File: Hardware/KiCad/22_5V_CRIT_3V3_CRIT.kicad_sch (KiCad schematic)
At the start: 0 parts

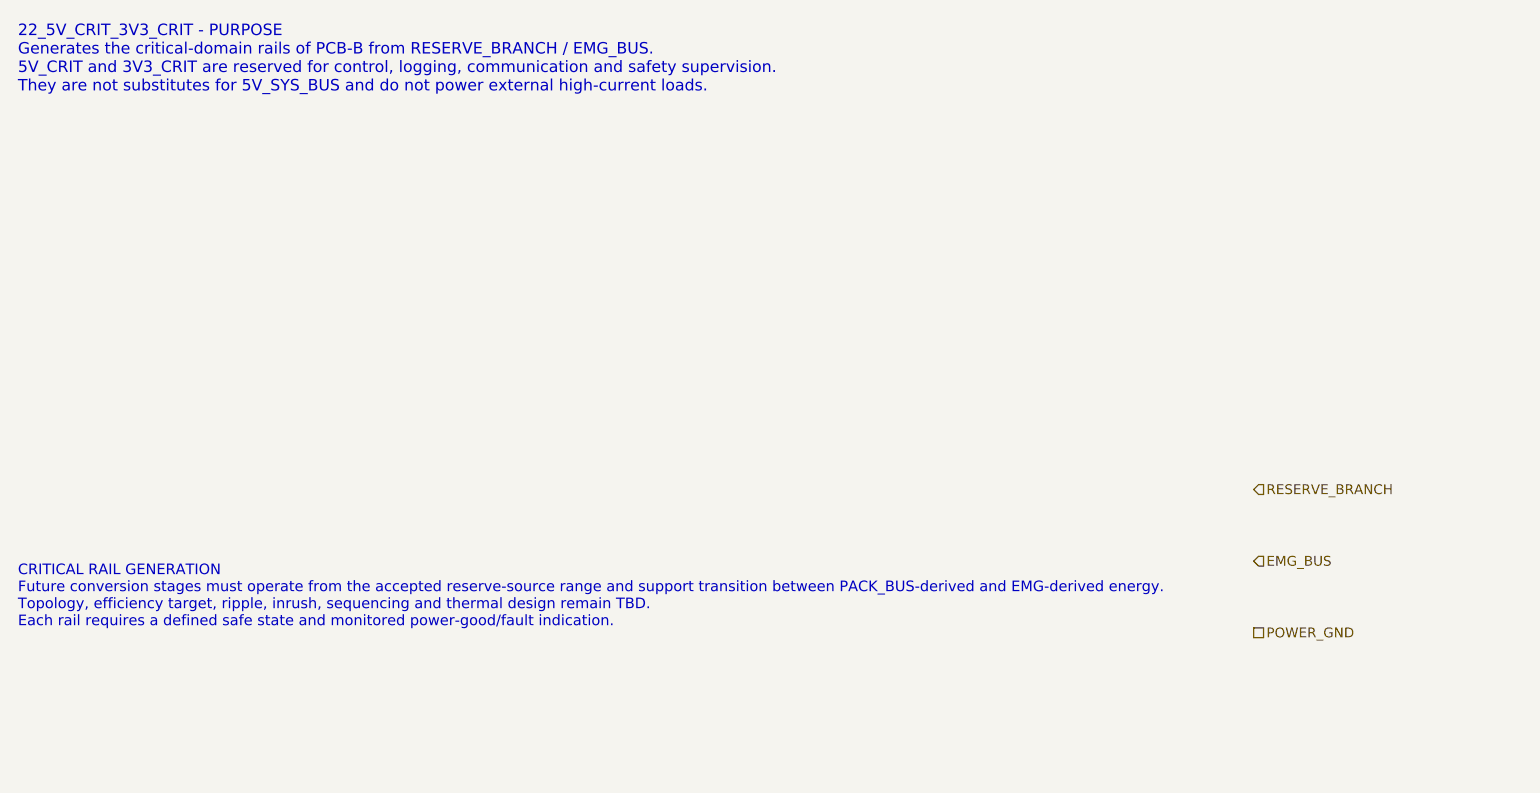
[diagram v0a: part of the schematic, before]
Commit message: hardware: align PCB-B CTRL_RESERVE interfaces
Merge PCB-B interface consistency fixes after verifying canonical names, diagnostics, and independent EXT_KILL final actions.
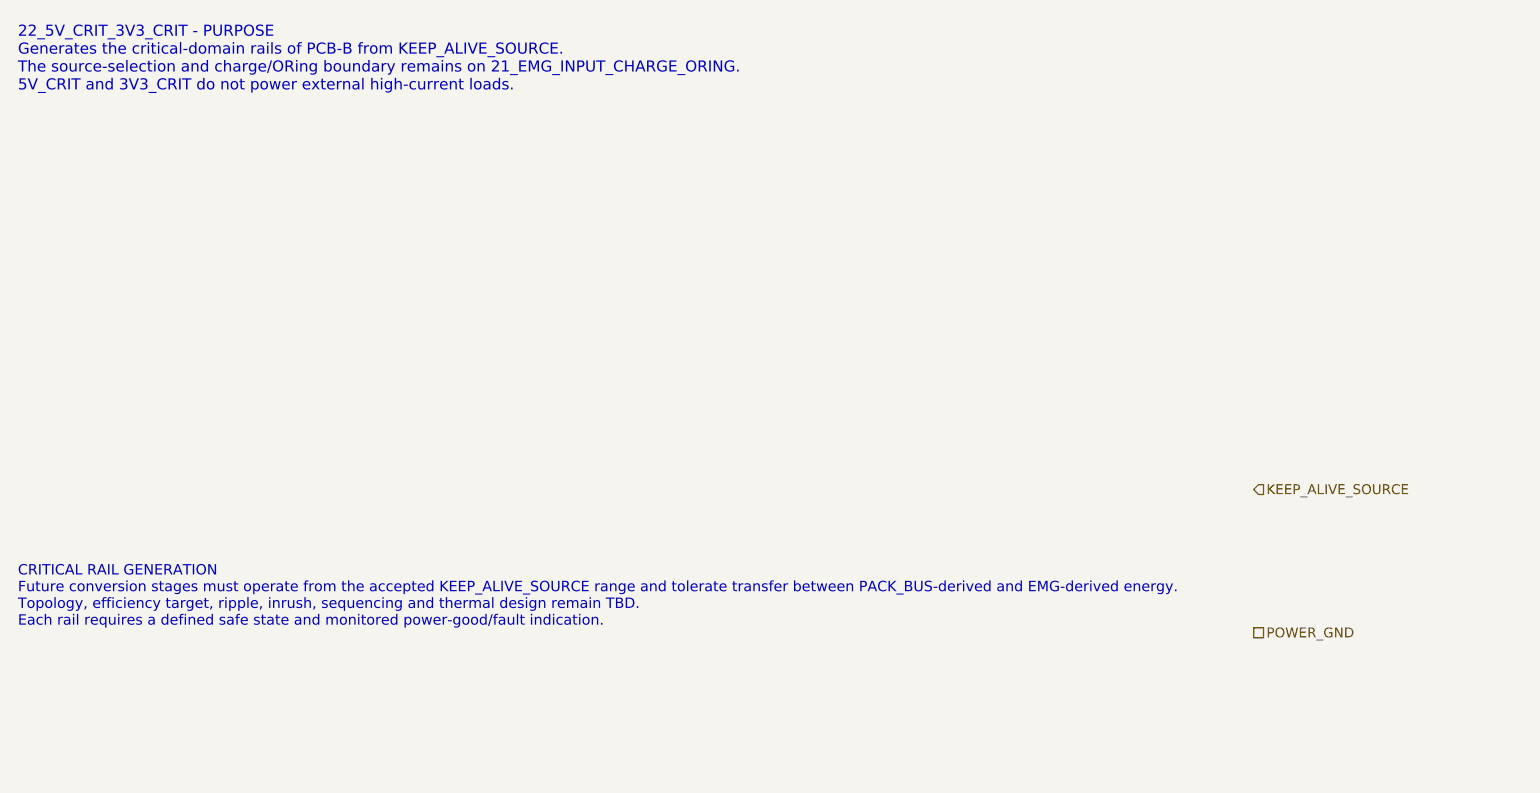
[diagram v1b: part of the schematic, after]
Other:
- note added: "22_5V_CRIT_3V3_CRIT - PURPOSE Generates the critical-domain rails of PCB-B from KEEP_ALIVE_SOURCE. The source-selection and charge/ORing boundary remains on 21_EMG_INPUT_CHARGE_ORING. 5V_CRIT and 3V3_CRIT do not power external high-current loads."
- note added: "CRITICAL RAIL GENERATION Future conversion stages must operate from the accepted KEEP_ALIVE_SOURCE range and tolerate transfer between PACK_BUS-derived and EMG-derived energy. Topology, efficiency target, ripple, inrush, sequencing and thermal design remain TBD. Each rail requires a defined safe state and monitored power-good/fault indication."
- note removed: "22_5V_CRIT_3V3_CRIT - PURPOSE Generates the critical-domain rails of PCB-B from RESERVE_BRANCH / EMG_BUS. 5V_CRIT and 3V3_CRIT are reserved for control, logging, communication and safety supervision. They are not substitutes for 5V_SYS_BUS and do not power external high-current loads."
- note removed: "CRITICAL RAIL GENERATION Future conversion stages must operate from the accepted reserve-source range and support transition between PACK_BUS-derived and EMG-derived energy. Topology, efficiency target, ripple, inrush, sequencing and thermal design remain TBD. Each rail requires a defined safe state and monitored power-good/fault indication."
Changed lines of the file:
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@@
 		(title "22_5V_CRIT_3V3_CRIT - critical-domain power conversion")
 		(date "2026-07-15")
-		(rev "B0")
+		(rev "B1")
 		(company "Gonoboben/plataVM")
-		(comment 1 "Architecture Level A/B: reserve-fed 5V_CRIT and 3V3_CRIT functional zones")
+		(comment 1 "Interface consistency: KEEP_ALIVE_SOURCE feeds critical rail generation")
 		(comment 2 "No DC/DC, LDO, supervisor, protection component, magnetics or footprint selected")
 	)
-	(text "22_5V_CRIT_3V3_CRIT - PURPOSE\nGenerates the critical-domain rails of PCB-B from RESERVE_BRANCH / EMG_BUS.\n5V_CRIT and 3V3_CRIT are reserved for control, logging, communication and safety supervision.\nThey are not substitutes for 5V_SYS_BUS and do not power external high-current loads."
+	(text "22_5V_CRIT_3V3_CRIT - PURPOSE\nGenerates the critical-domain rails of PCB-B from KEEP_ALIVE_SOURCE.\nThe source-selection and charge/ORing boundary remains on 21_EMG_INPUT_CHARGE_ORING.\n5V_CRIT and 3V3_CRIT do not power external high-current loads."
 		(exclude_from_sim no)
 		(at 12 14 0)
-		(effects (font (size 1.28 1.28)) (justify left))
+		(effects (font (size 1.24 1.24)) (justify left))
 		(uuid "ctrl-reserve-00000022-0000-4000-8000-000000000101")
 	)
-	(text "CRITICAL RAIL GENERATION\nFuture conversion stages must operate from the accepted reserve-source range and support transition between PACK_BUS-derived and EMG-derived energy.\nTopology, efficiency target, ripple, inrush, sequencing and thermal design remain TBD.\nEach rail requires a defined safe state and monitored power-good/fault indication."
+	(text "CRITICAL RAIL GENERATION\nFuture conversion stages must operate from the accepted KEEP_ALIVE_SOURCE range and tolerate transfer between PACK_BUS-derived and EMG-derived energy.\nTopology, efficiency target, ripple, inrush, sequencing and thermal design remain TBD.\nEach rail requires a defined safe state and monitored power-good/fault indication."
 		(exclude_from_sim no)
 		(at 12 74 0)
-		(effects (font (size 1.18 1.18)) (justify left))
+		(effects (font (size 1.16 1.16)) (justify left))
 		(uuid "ctrl-reserve-00000022-0000-4000-8000-000000000102")
 	)
@@
 		(uuid "ctrl-reserve-00000022-0000-4000-8000-000000000104")
 	)
-	(hierarchical_label "RESERVE_BRANCH" (shape input) (exclude_from_sim no) (at 150 62 0) (effects (font (size 1.1 1.1)) (justify left)) (uuid "ctrl-reserve-00000022-0000-4000-8000-000000000201"))
-	(hierarchical_label "EMG_BUS" (shape input) (exclude_from_sim no) (at 150 70 0) (effects (font (size 1.1 1.1)) (justify left)) (uuid "ctrl-reserve-00000022-0000-4000-8000-000000000202"))
+	(hierarchical_label "KEEP_ALIVE_SOURCE" (shape input) (exclude_from_sim no) (at 150 62 0) (effects (font (size 1.1 1.1)) (justify left)) (uuid "ctrl-reserve-00000022-0000-4000-8000-000000000201"))
 	(hierarchical_label "POWER_GND" (shape passive) (exclude_from_sim no) (at 150 78 0) (effects (font (size 1.1 1.1)) (justify left)) (uuid "ctrl-reserve-00000022-0000-4000-8000-000000000203"))
 	(hierarchical_label "5V_CRIT" (shape output) (exclude_from_sim no) (at 150 122 0) (effects (font (size 1.1 1.1)) (justify left)) (uuid "ctrl-reserve-00000022-0000-4000-8000-000000000204"))
